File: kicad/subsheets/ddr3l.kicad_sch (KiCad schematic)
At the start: 29 parts, among them U6 MT41K256M16TW-107:P

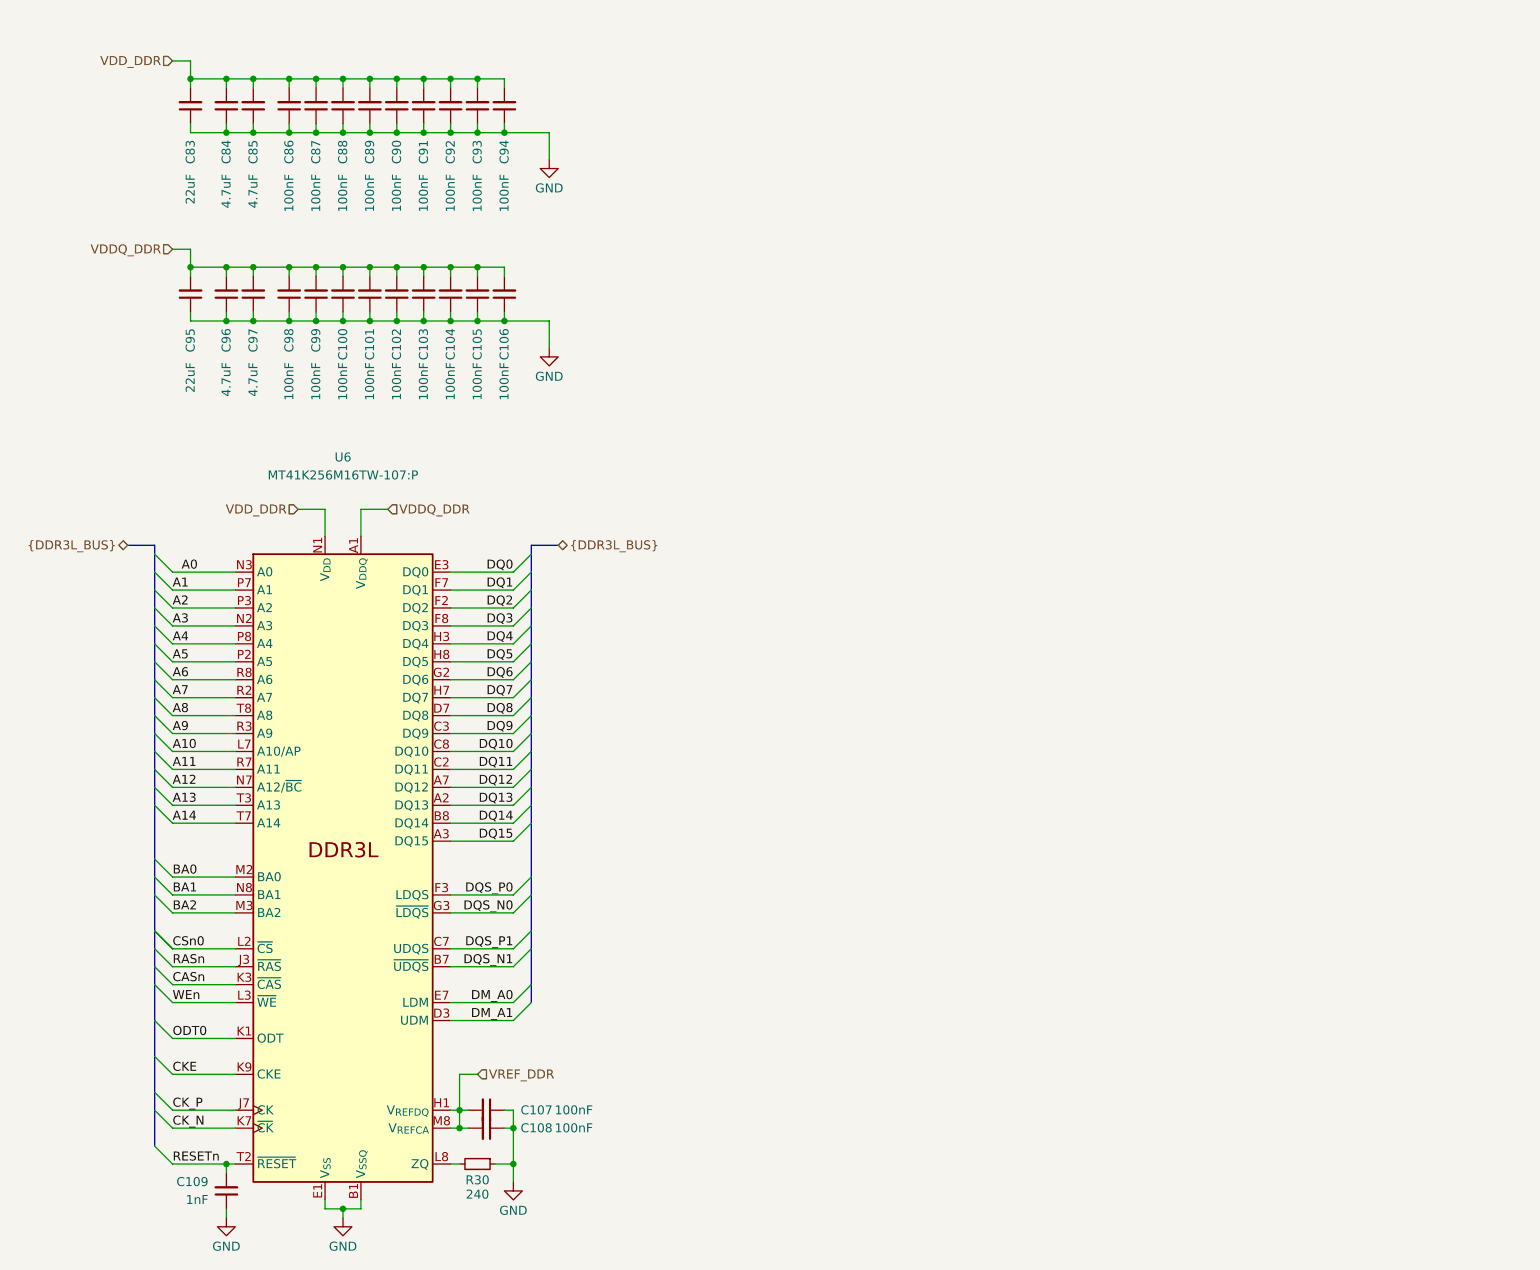
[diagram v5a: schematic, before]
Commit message: Change all sheets to A4, name sheets, split RK3566 into hierarchy
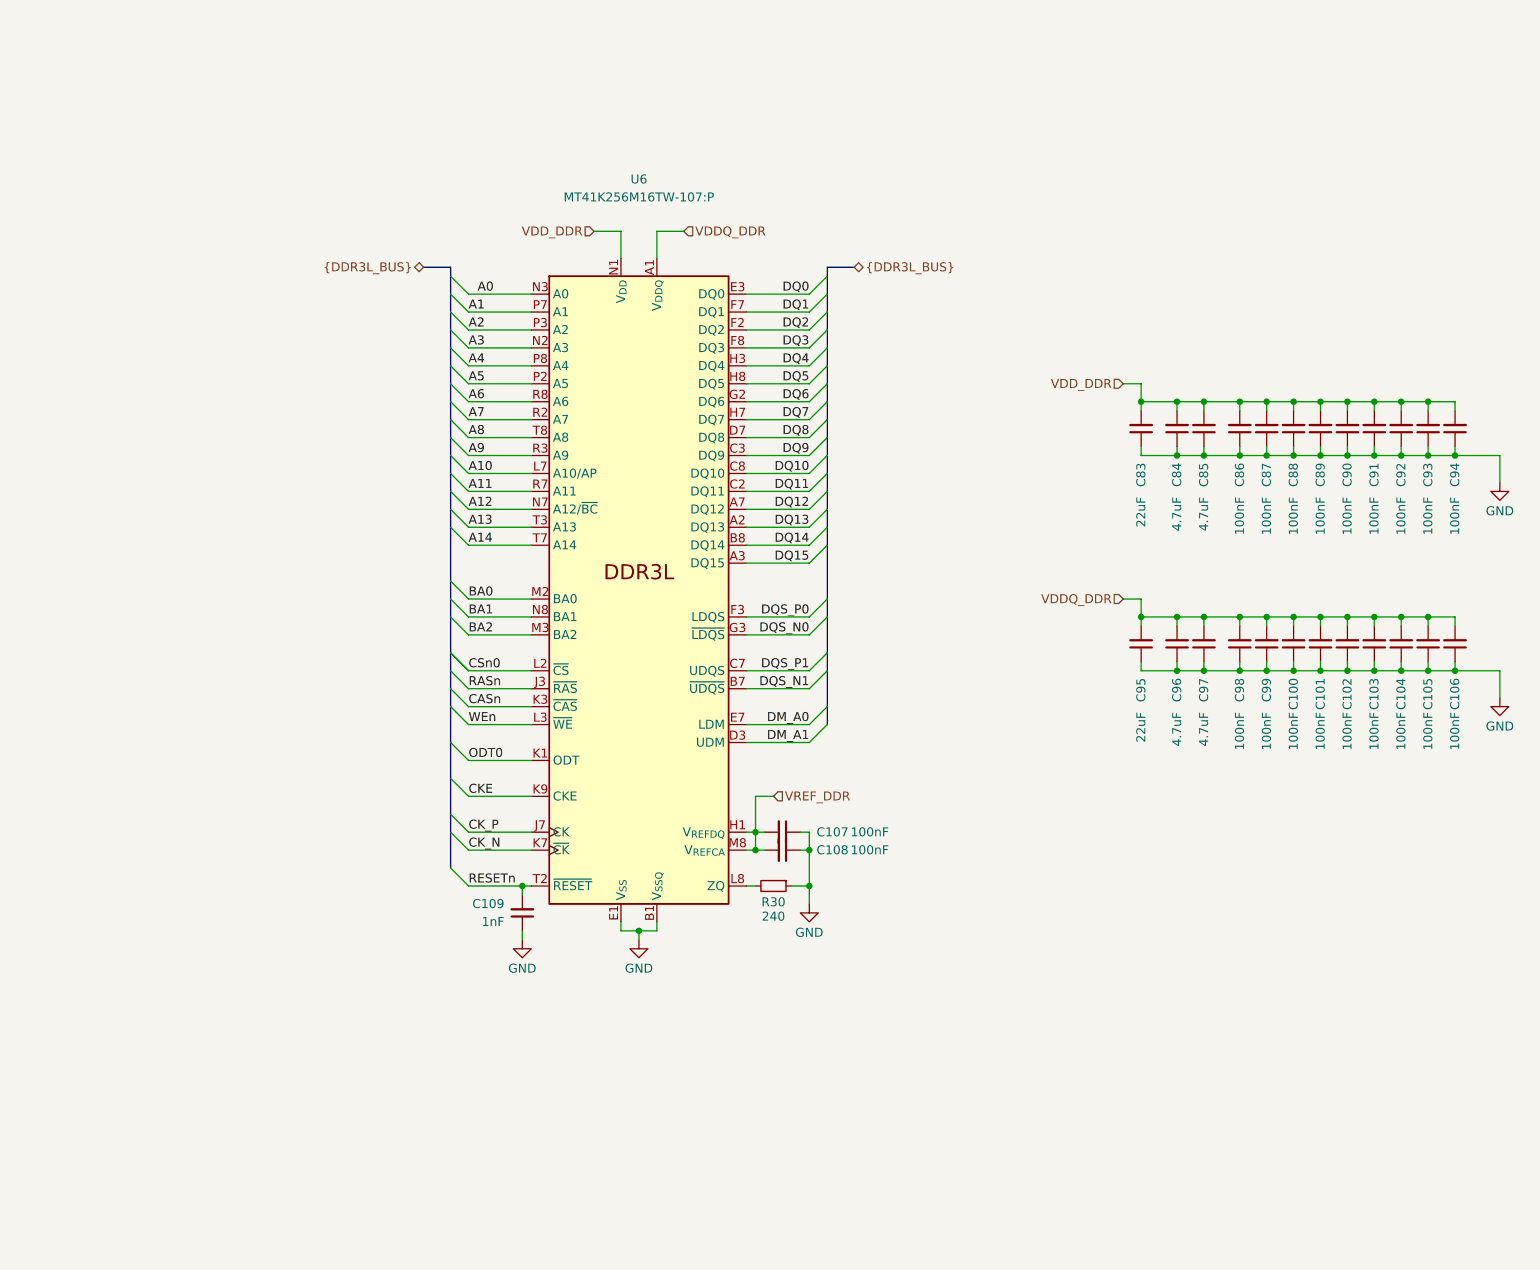
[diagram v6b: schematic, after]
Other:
- title: (none) -> DDR3L Memory
- moved on the sheet: C100, C101, C102, C103, C104, C105, C106, C107, C108, C109, C83, C84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

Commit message: Mark as R1.0
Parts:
- renumbered C83 to C126, C84 to C127, C85 to C128, C86 to C129, C87 to C130, C88 to C131, C89 to C132, C90 to C133, C91 to C134, C92 to C135, C93 to C136, C94 to C137, C95 to C138, C96 to C139, C97 to C140, C98 to C141, C99 to C142, C100 to C143, C101 to C144, C102 to C145, C103 to C146, C104 to C147, C105 to C148, C106 to C149, C107 to C150, C108 to C151, C109 to C152, R30 to R46
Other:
- company: (none) -> UVic Rocketry

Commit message: Annotations
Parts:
- removed C150, C151: 100nF, symbol Device:C_Small
- added C163, C164, C165: 100nF, symbol Device:C_Small
- added R49, R50: 10k, symbol Device:R_Small
- added R51, R52: 240, symbol Device:R_Small
- renumbered C126 to C139, C127 to C140, C128 to C141, C129 to C142, C130 to C143, C131 to C144, C132 to C145, C133 to C146, C134 to C147, C135 to C148, C136 to C149, C137 to C150, C138 to C151, C139 to C152, C140 to C153, C141 to C154, C142 to C155, C143 to C156, C144 to C157, C145 to C158, C146 to C159, C147 to C160, C148 to C161, C149 to C162, C152 to C166, R46 to R53
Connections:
- net GND: now also C163.2, C164.2, C165.2, R50.2
- net VDD_DDR: now also C163.1, R49.1
- net VREF_DDR: now also R51.1; no longer U6.H1 (V_{REFDQ}), U6.M8 (V_{REFCA})
- new net: C165.1, R51.2, U6.H1 (V_{REFDQ})
- new net: C164.1, R52.2, U6.M8 (V_{REFCA})
- new net +0.675V: R49.2, R50.1, R52.1
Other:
- moved on the sheet: C139, C140, C141, C142, C143, C144, C145, C146, C147, C148, C149, C150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
